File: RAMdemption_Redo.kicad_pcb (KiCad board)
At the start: 4 copper layers, 99 x 53.5 mm, 41 parts, among them J1 Conn_RAM_Expansion, U1 TC518512FTL-70, U10 TC518512FTL-70, U11 TC518512FTL-70, U12 TC518512FTL-70, U13 TC518512FTL-70, U14 TC518512FTL-70, U15 TC518512FTL-70, U16 TC518512FTL-70, U17 TC518512FTL-70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

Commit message: preliminary power routing
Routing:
- net +5V: track 339.8 -> 420.1 mm, vias 23 -> 28
- net GND: track 64.9 -> 113.7 mm, vias 19 -> 21

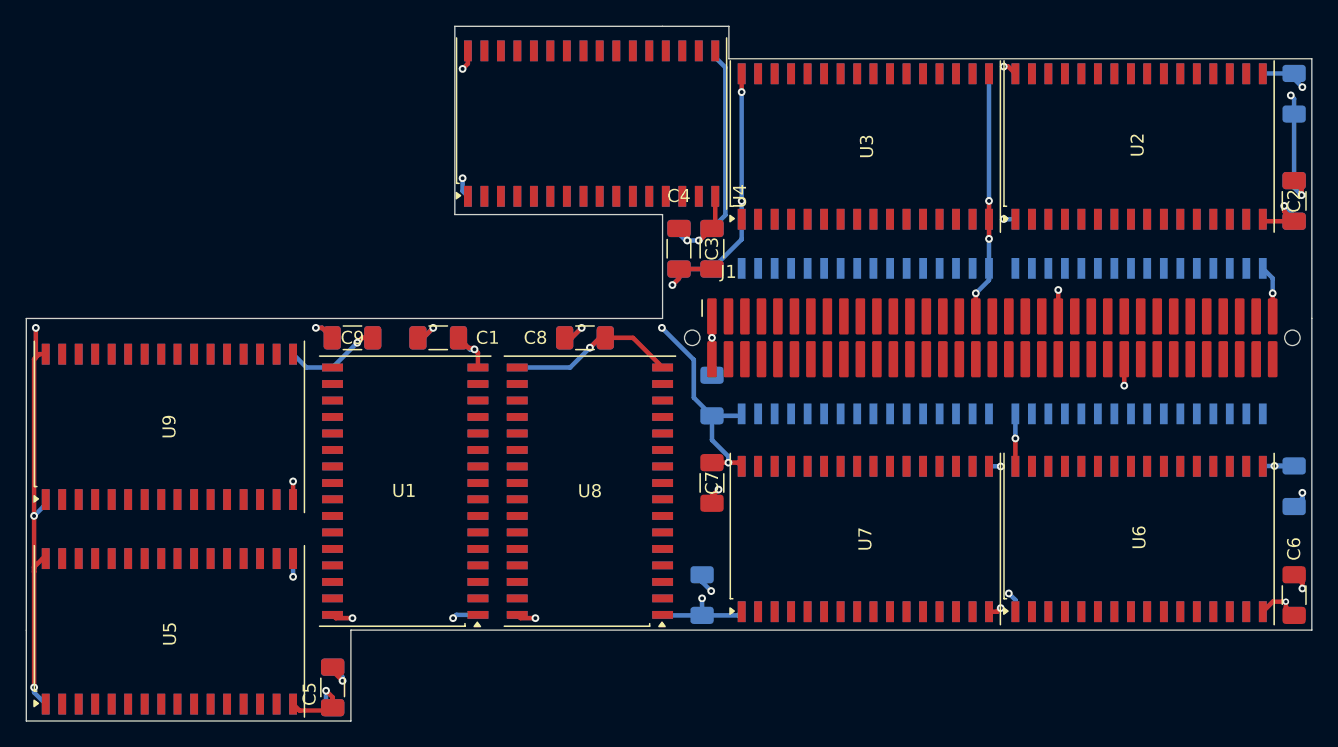
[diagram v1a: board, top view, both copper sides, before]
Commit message: fix up positions of U10, U14, U18 etc
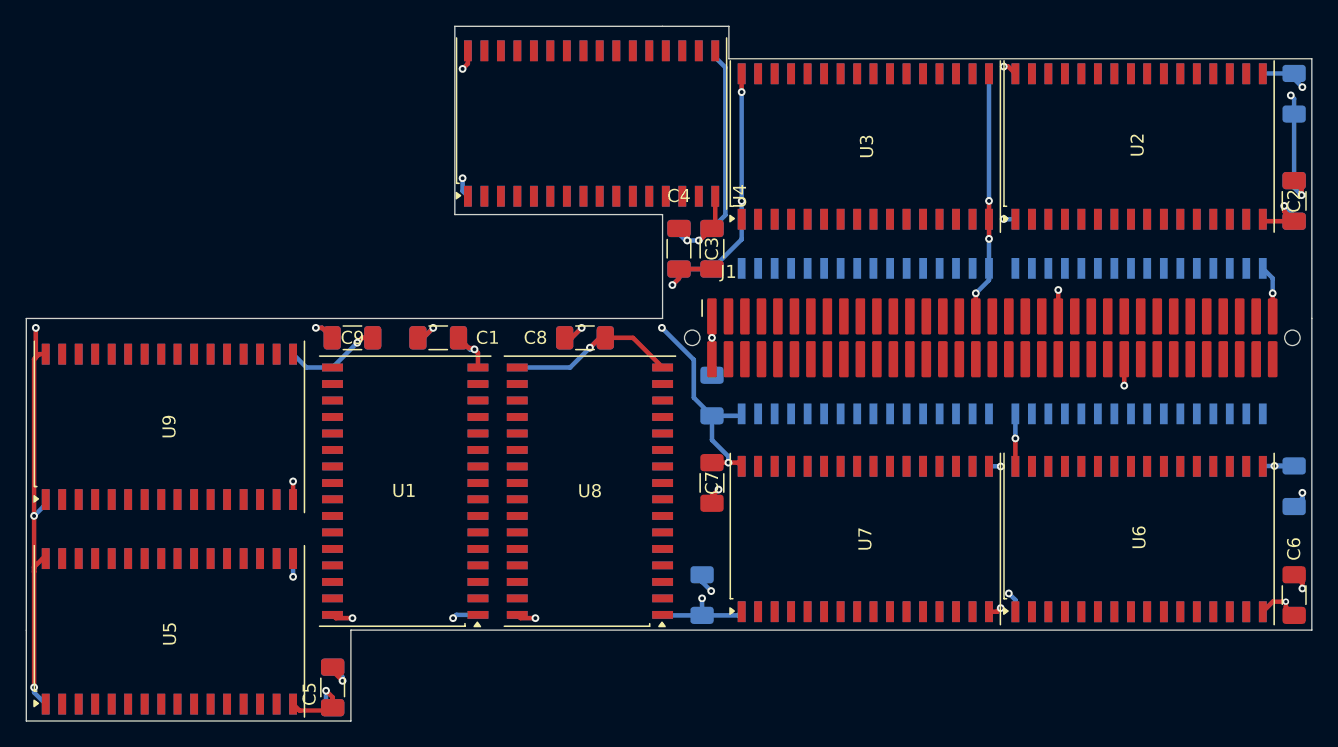
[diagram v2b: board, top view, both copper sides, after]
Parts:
- moved U18 62.4 mm to (196.8, 88.8), turned to -90 degrees
- moved U16 57.7 mm to (140.3, 115.3), turned to 0 degrees
- moved U10 52.9 mm to (196.8, 119.0)
- moved U14 43.8 mm to (196.8, 103.8), turned to -90 degrees
- moved U12 42.5 mm to (154.5, 115.3), turned to 0 degrees
- moved U20 42.2 mm to (154.7, 87.0)

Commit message: progress!
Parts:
- moved C16 0.25 mm to (163.7, 107.9)
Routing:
- net /RAM Bank 1/A18: track 0.00 -> 167.0 mm, vias 0 -> 13
- net /RAM Bank 1/A16: track 0.00 -> 162.3 mm, vias 0 -> 12
- net /RAM Bank 1/A14: track 0.00 -> 159.3 mm, vias 0 -> 12
- net /RAM Bank 1/A12: track 0.00 -> 158.1 mm, vias 0 -> 12
- net /RAM Bank 1/A7: track 0.00 -> 157.2 mm, vias 0 -> 12
- net /RAM Bank 1/A6: track 0.00 -> 156.3 mm, vias 0 -> 12
- net /RAM Bank 1/A5: track 0.00 -> 155.5 mm, vias 0 -> 12
- net /RAM Bank 1/A4: track 0.00 -> 154.9 mm, vias 0 -> 12
- net /RAM Bank 1/A3: track 0.00 -> 153.8 mm, vias 0 -> 12
- net /RAM Bank 1/A2: track 0.00 -> 152.9 mm, vias 0 -> 12
- net /RAM Bank 1/A15: track 0.00 -> 152.1 mm, vias 0 -> 12
- net /RAM Bank 1/A0: track 0.00 -> 151.9 mm, vias 0 -> 12
- net /RAM Bank 1/A1: track 0.00 -> 151.7 mm, vias 0 -> 12
- net /RAM Bank 1/A17: track 0.00 -> 150.0 mm, vias 0 -> 12
- net /RAM Bank 1/A13: track 0.00 -> 147.0 mm, vias 0 -> 12
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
